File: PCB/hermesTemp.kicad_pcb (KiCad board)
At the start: 2 copper layers, 55 x 43 mm, 20 parts, among them P1 LOGO, P2 LOGO, U1 N069-9616TSWPG02-H14, U2 AHT20, U3 STM32F103C8T6

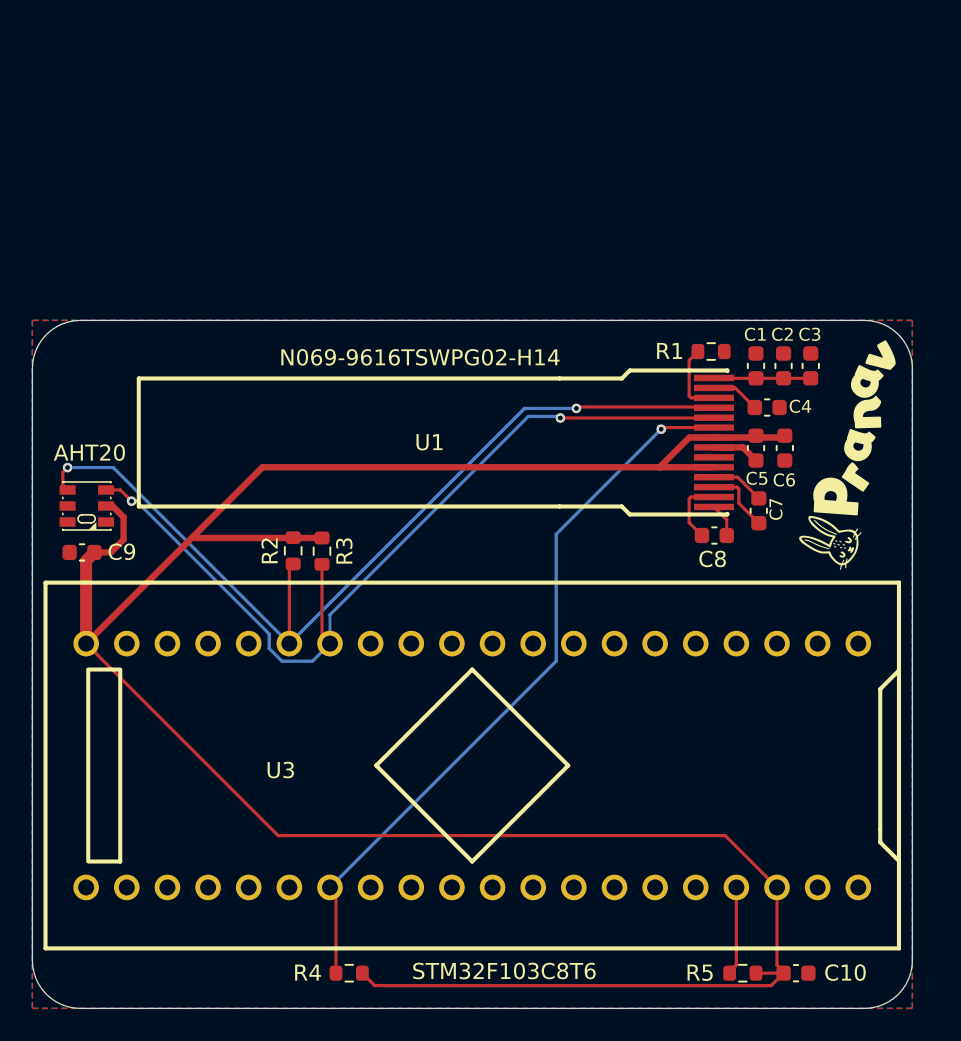
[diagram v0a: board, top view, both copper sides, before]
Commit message: Update based on reviewer feedback.
Switched to XIAO RP2040 (dropped STM32 + PCBA for MCU/OLED) to simplify design and reduce cost. Increased project complexity by adding STK8328 accelerometer and AGR10 pressure sensor alongside AHT20. Updated schematic and firmware to support multi-sensor setup (I2C + analog) and display all data on OLED.
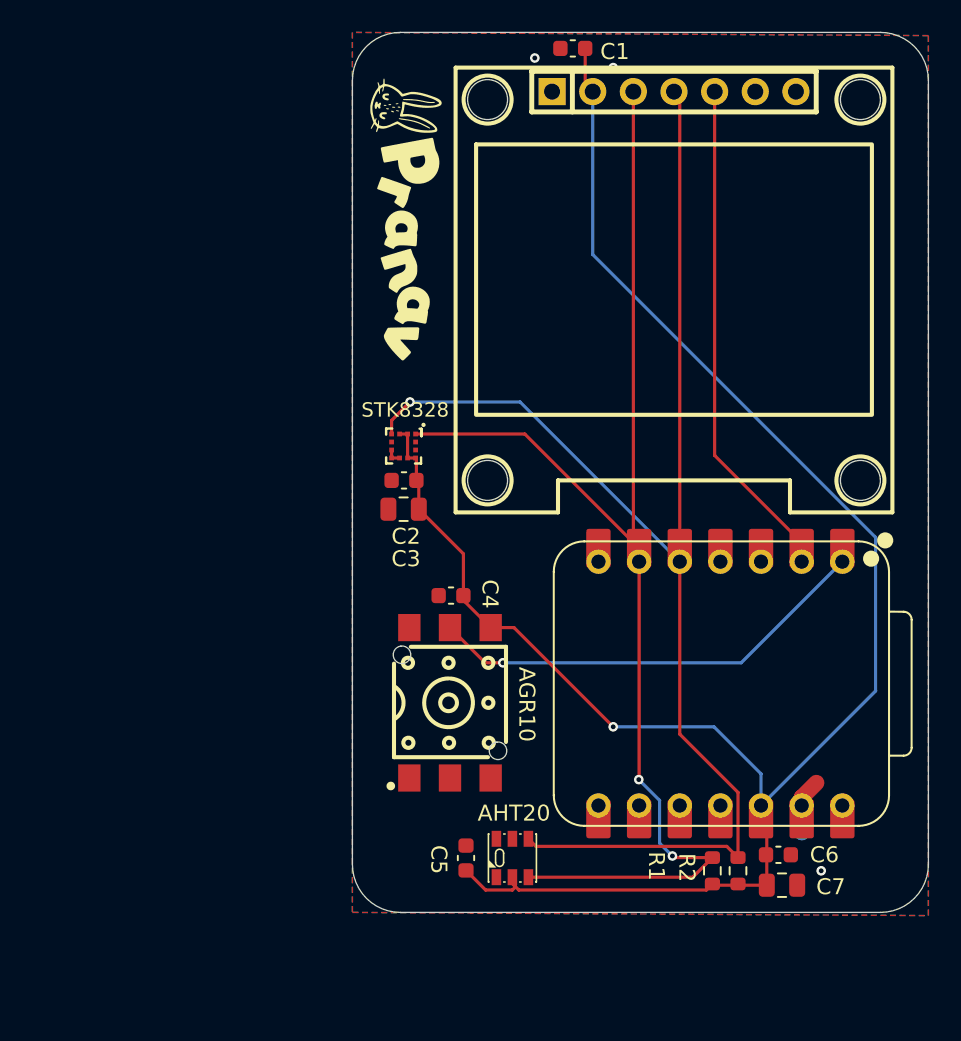
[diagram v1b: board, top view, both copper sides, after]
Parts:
- removed C10: 10uF, Capacitor_SMD:C_0603_1608Metric
- removed C8: 1uF, Capacitor_SMD:C_0603_1608Metric
- removed C9: 0.1uF, Capacitor_SMD:C_0603_1608Metric
- removed P1: LOGO, LOGO
- removed R3: 4.7k, Resistor_SMD:R_0603_1608Metric
- removed R4, R5: 10k, Resistor_SMD:R_0603_1608Metric
- added G***: LOGO, LOGO, F.Cu at (144.3, 72.0)
- added OLED1: ~, hermesExtraFoot:OLED-TH_HS96L01W4S03, F.Cu at (161.1, 64.0)
- added U4: AHT20, hermesExtraFoot:SENSOR-SMD-6_AHT20, F.Cu at (151.0, 111.9)
- C2: value 2.2uF -> 0.1uF
- C3: value 4.7uF -> 10uF; footprint Capacitor_SMD:C_0603_1608Metric -> Capacitor_SMD:C_0805_2012Metric
- C4: value 1uF -> 0.1uF
- C6: value 4.7uF -> 0.1uF
- C7: value 1uF -> 10uF; footprint Capacitor_SMD:C_0603_1608Metric -> Capacitor_SMD:C_0805_2012Metric
- R1: value 1M -> 4.7k
- U1: value N069-9616TSWPG02-H14 -> STK8328; footprint hermesExtraFoot:LCD-SMD_N069-9616TSWPG02-H14 -> hermesExtraFoot:VLGA-12_L2.0-W2.0-P0.50-BL
- U2: value AHT20 -> XIAO-RP2040-DIP; footprint hermesExtraFoot:SENSOR-SMD-6_AHT20 -> hermesExtraFoot:XIAO-RP2040-DIP
- U3: value STM32F103C8T6 -> AGR10; footprint hermesExtraFoot:STM32F103C8T6 -> hermesExtraFoot:KEY-SMD_6P-L7.0-W7.0-P2.54-LS10.6
- moved U2 41.1 mm to (164.0, 101.0), turned to 0 degrees
- moved R2 34.2 mm to (165.1, 112.7), turned to -90 degrees
- moved R1 32.5 mm to (163.5, 112.7), turned to 90 degrees
- moved C5 31.4 mm to (148.1, 111.9), turned to -90 degrees
- moved C3 27.0 mm to (144.2, 90.1), turned to 180 degrees
- moved C6 25.4 mm to (167.6, 111.7), turned to 180 degrees
- moved C2 24.8 mm to (144.2, 88.3), turned to 0 degrees
- moved C7 23.4 mm to (167.8, 113.6), turned to 180 degrees
- moved C4 23.0 mm to (147.2, 95.5)
- moved C1 22.9 mm to (154.8, 61.3), turned to 0 degrees
- moved U1 19.4 mm to (144.2, 86.2), turned to 180 degrees
- moved U3 4.16 mm to (147.1, 102.2), turned to 90 degrees
- moved P2 2.91 mm to (149.2, 89.8), turned to -90 degrees
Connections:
- C1 pad 2: VCCOLED -> +3V3
- C2 pad 2: VCCOLED -> +3V3
- C3 pad 1: GND -> +3V3
- C3 pad 2: VCCOLED -> GND
- C4 pad 1: Net-(U1-VCOMH) -> GND
- C4 pad 2: GND -> +3V3
- C7 pad 1: Net-(U1-C1N) -> GND
- C7 pad 2: Net-(U1-C1P) -> +3V3
- R1 pad 1: Net-(U1-IREF) -> +3V3
- R1 pad 2: GND -> SCL
- U1 pad 1: Net-(U1-C2P) -> SCL
- U1 pad 10: SCL -> +3V3
- U1 pad 11: SDA -> unconnected-(U1-INT2-Pad11)
- U1 pad 12: Net-(U1-IREF) -> unconnected-(U1-INT1-Pad12)
- U1 pad 2: Net-(U1-C2N) -> +3V3
- U1 pad 3: Net-(U1-C1P) -> +3V3
- U1 pad 4: Net-(U1-C1N) -> SDA
- U1 pad 5: +3V3 -> unconnected-(U1-NC-Pad5)
- U1 pad 6: unconnected-(U1-VBREF-Pad6) -> GND
- U1 pad 8: +3V3 -> GND
- U1 pad 9: RES -> +3V3
- U2 pad 1: unconnected-(U2-NC-Pad1) -> AGRANALOG
- U2 pad 2: +3V3 -> OLED_RES
- U2 pad 3: SCL -> unconnected-(U2-P28_A2_D2-Pad3)
- U2 pad 4: SDA -> unconnected-(U2-P29_A3_D3-Pad4)
- U2 pad 5: GND -> SDA
- U2 pad 6: unconnected-(U2-NC-Pad6) -> SCL
- U3 pad 1: unconnected-(U3-PB12-Pad1) -> GND
- U3 pad 2: unconnected-(U3-PB13-Pad2) -> GND
- U3 pad 4: unconnected-(U3-PB15-Pad4) -> +3V3
- U3 pad 5: unconnected-(U3-PA8-Pad5) -> AGRANALOG
- U3 pad 6: unconnected-(U3-PA9-Pad6) -> GND
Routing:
- net RES: track 46.1 -> 0.00 mm, vias 1 -> 0
- net +3V3: track 155.1 -> 121.0 mm, vias 0 -> 1
- net OLED_RES: track 0.00 -> 30.8 mm
- net SDA: track 57.8 -> 87.4 mm, vias 2 -> 1
- net AGRANALOG: track 0.00 -> 28.0 mm, vias 0 -> 1
- net SCL: track 55.6 -> 80.3 mm
- net VCCOLED: track 6.06 -> 0.00 mm
- net Net-(U3-RESET): track 5.54 -> 0.00 mm
- net Net-(U1-IREF): track 4.60 -> 0.00 mm
- net Net-(U1-C1P): track 4.25 -> 0.00 mm
- net Net-(U1-C2N): track 4.22 -> 0.00 mm
- net Net-(U1-C1N): track 3.35 -> 0.00 mm
- net Net-(U1-VCOMH): track 3.06 -> 0.00 mm
- net Net-(U1-C2P): track 2.12 -> 0.00 mm
- net GND: track 2.96 -> 4.49 mm, vias 0 -> 3
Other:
- board size 55 x 43 mm -> 36 x 55 mm

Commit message: Build review update
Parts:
- U2: value XIAO-RP2040-DIP -> RP2040-ZERO; footprint hermesExtraFoot:XIAO-RP2040-DIP -> hermesExtraFoot:MODULE_RP2040-ZERO
- U3: value AGR10 -> ~; footprint hermesExtraFoot:KEY-SMD_6P-L7.0-W7.0-P2.54-LS10.6 -> hermesExtraFoot:LGA-8_L3.8-W3.6-P0.90-TL_WF183D
- moved C5 19.8 mm to (155.1, 93.4)
- moved U4 19.8 mm to (158.0, 93.4)
- moved C6 19.4 mm to (170.9, 92.6)
- moved C7 19.4 mm to (171.2, 94.5)
- moved R1 19.4 mm to (166.8, 93.6)
- moved R2 19.4 mm to (168.4, 93.6)
- moved U2 3.93 mm to (164.7, 104.9), turned to -90 degrees
- moved U3 2.60 mm to (147.2, 99.6), turned to -90 degrees
- moved P2 1.36 mm to (148.3, 88.8)
- moved G*** 0.51 mm to (144.2, 72.5)
- moved C4 0.14 mm to (147.3, 95.5), turned to 180 degrees
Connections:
- U2 pad 1: AGRANALOG -> unconnected-(U2-GP0-Pad1)
- U2 pad 12: +3V3 -> unconnected-(U2-GP11-Pad12)
- U2 pad 13: GND -> unconnected-(U2-GP12-Pad13)
- U2 pad 2: OLED_RES -> unconnected-(U2-GP1-Pad2)
- U2 pad 7: unconnected-(U2-P0_D6_TX-Pad7) -> OLED_RES
- U3 pad 1: GND -> SCL
- U3 pad 3: unconnected-(U3-NC-Pad3) -> +3V3
- U3 pad 4: +3V3 -> unconnected-(U3-VS-Pad4)
- U3 pad 5: AGRANALOG -> unconnected-(U3-RX-Pad5)
- U3 pad 6: GND -> unconnected-(U3-TX-Pad6)
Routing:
- net SCL: track 80.3 -> 110.4 mm, vias 2 -> 3
- net OLED_RES: track 30.8 -> 59.9 mm
- net AGRANALOG: track 28.0 -> 0.00 mm, vias 1 -> 0
- net SDA: track 87.4 -> 104.2 mm, vias 1 -> 2
- net +3V3: track 121.0 -> 112.0 mm, vias 1 -> 3
- net GND: track 4.49 -> 1.00 mm, vias 3 -> 5
